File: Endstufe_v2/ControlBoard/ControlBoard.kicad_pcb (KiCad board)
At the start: 4 copper layers, 100 x 85 mm, 231 parts, among them J1 B4B-XH-2_(LF)(SN), J10 DNP, J11 DNP, J12 DNP, J13 DNP, J14 DAC all outputs, J15 B4B-XH-2_(LF)(SN), J16 B6B-XH-2(LF)(SN), J17 Conn_01x02_Pin, J18 Conn_01x02_Pin, J19 Conn_01x06_Pin, J2 B4B-XH-2_(LF)(SN), J3 B4B-XH-2_(LF)(SN), J4 DNP, J5 B6B-XH-2(LF)(SN), J6 Conn_01x02_Pin, J7 DNP, J8 DNP, J9 DNP, SW1 TS-1187A-B-A-B, SW2 TS-1187A-B-A-B, U1 NVTFWS014P04M8LTAG, U10 ADAU1962AWBSTZ, U2 1SMA5927A, U3 TPS62933, U4 TYPE-C 16PFS 2JCB1.2-H6.5 IPX8, U5 W25Q128JVS, U6 RP2040, U7 W25Q128JVS, U8 ADAU1467WBCPZ300, U9 ZPLR135_T8, Y1 12Mhz, Y2 24.576Mhz, Y3 24.576Mhz

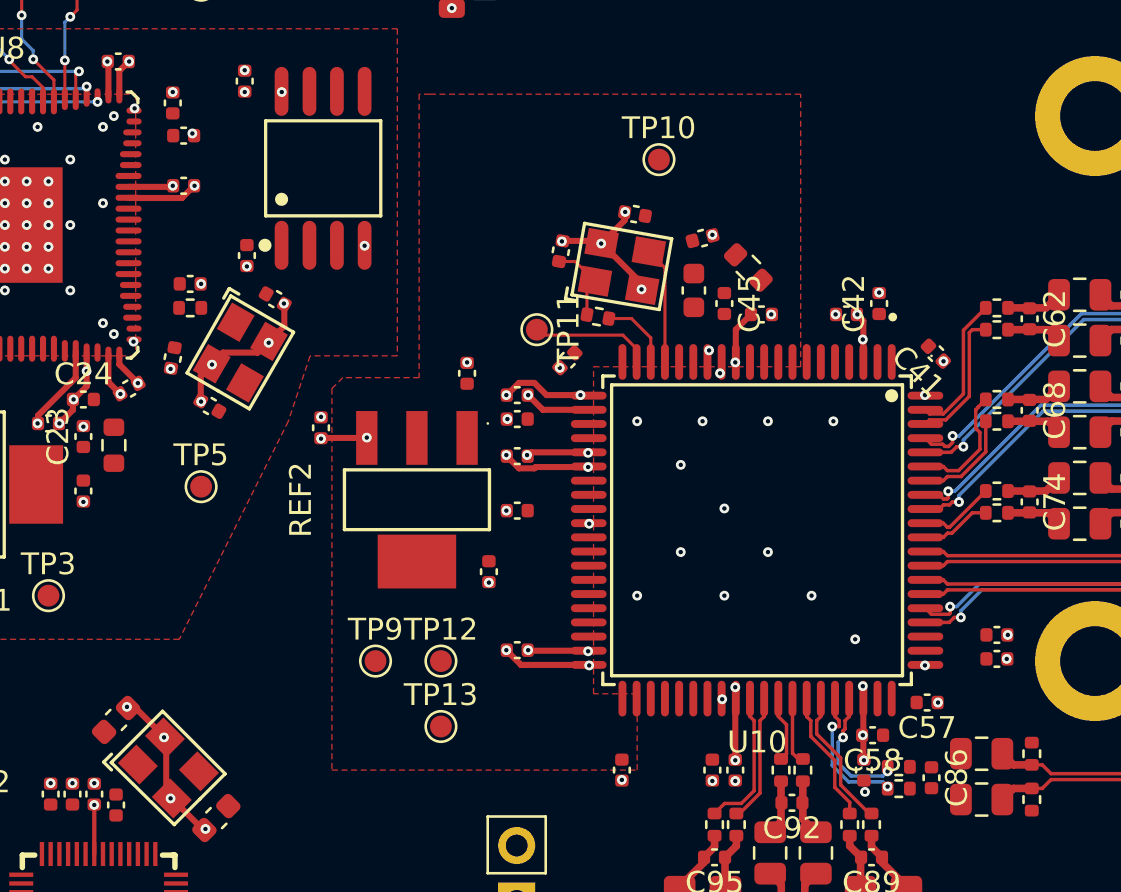
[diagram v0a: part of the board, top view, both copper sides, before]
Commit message: Route control board (continued)
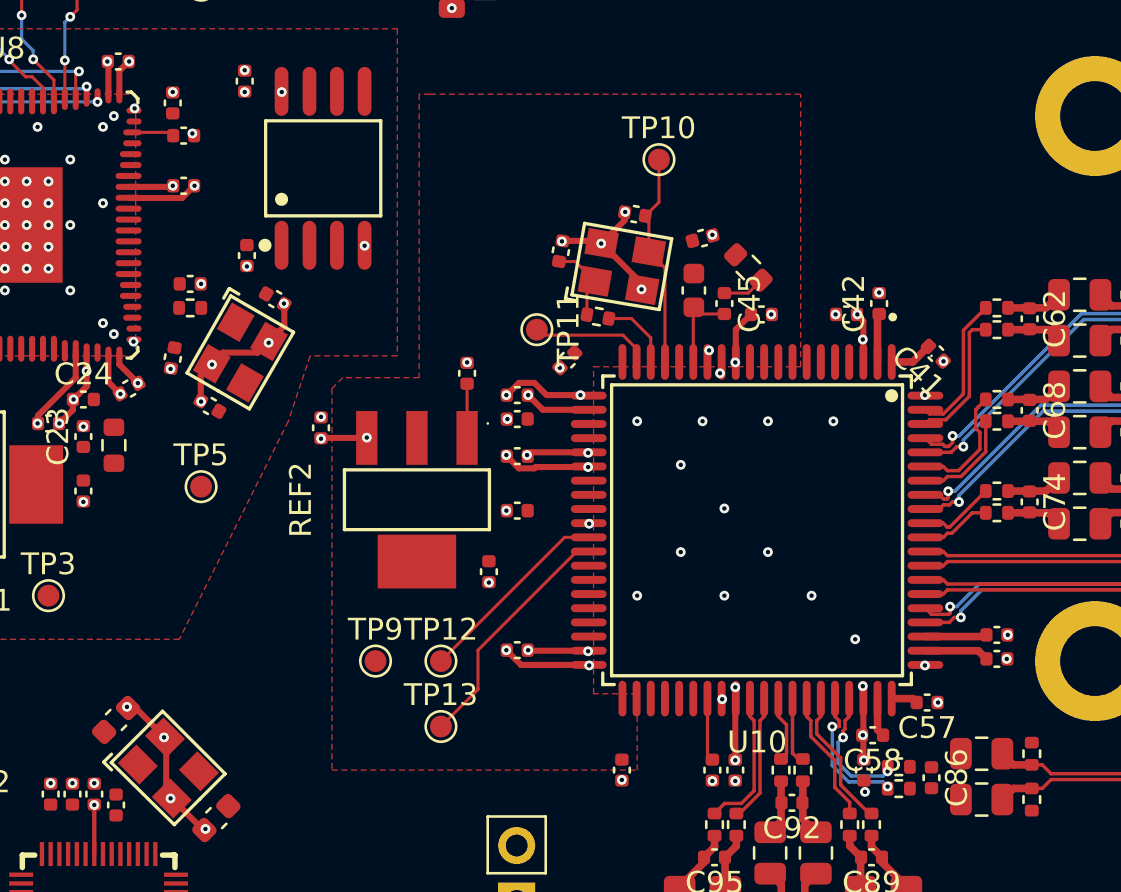
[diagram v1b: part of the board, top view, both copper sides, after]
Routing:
- net Net-(U10-SA2): track 0.00 -> 11.2 mm
- net Net-(U10-SA1): track 0.00 -> 9.13 mm
- net /ADAU1962A/XTALI: track 5.36 -> 9.91 mm
- net /ADAU1962A/LF: track 0.00 -> 4.04 mm
- net /ADAU1962A/CM: track 0.00 -> 2.95 mm
- net /ADAU1962A_RESET: track 0.00 -> 2.89 mm
- net /ADAU1962A/TS_REF: track 0.00 -> 2.83 mm
- net /ADAU1962A/VDRIVE: track 0.00 -> 2.49 mm
- net /ADAU1962A/DAC_BIAS4: track 0.00 -> 2.23 mm
- net /ADAU1962A/DAC_BIAS3: track 0.00 -> 1.98 mm
- net Net-(U8-SELFBOOT): track 0.00 -> 1.93 mm
- net Net-(C45-Pad1): track 0.00 -> 1.93 mm
- net /ADAU1962A/DAC_BIAS1: track 0.00 -> 1.78 mm
- net /ADAU1962A/DAC_BIAS2: track 0.00 -> 1.22 mm

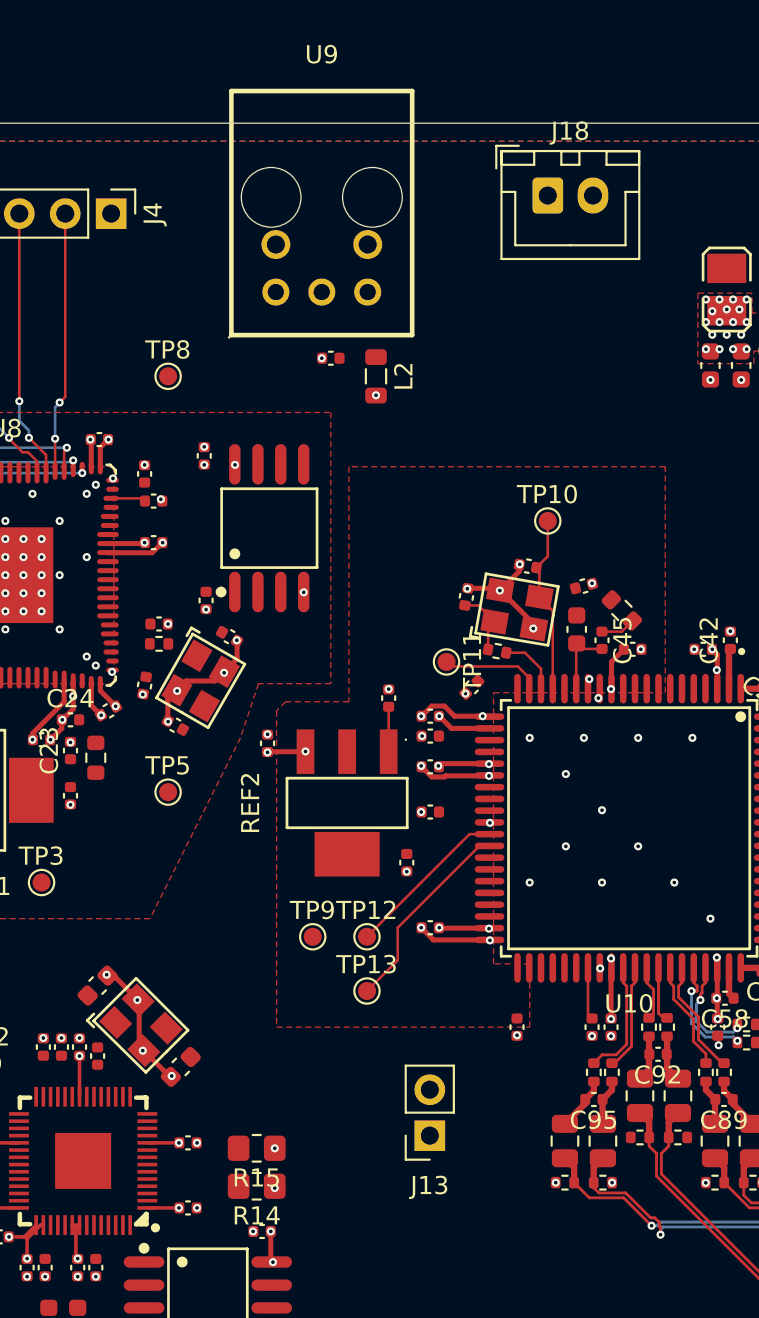
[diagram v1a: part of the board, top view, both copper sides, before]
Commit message: Add missing I2C adress headers and pull down for DAC and DSP
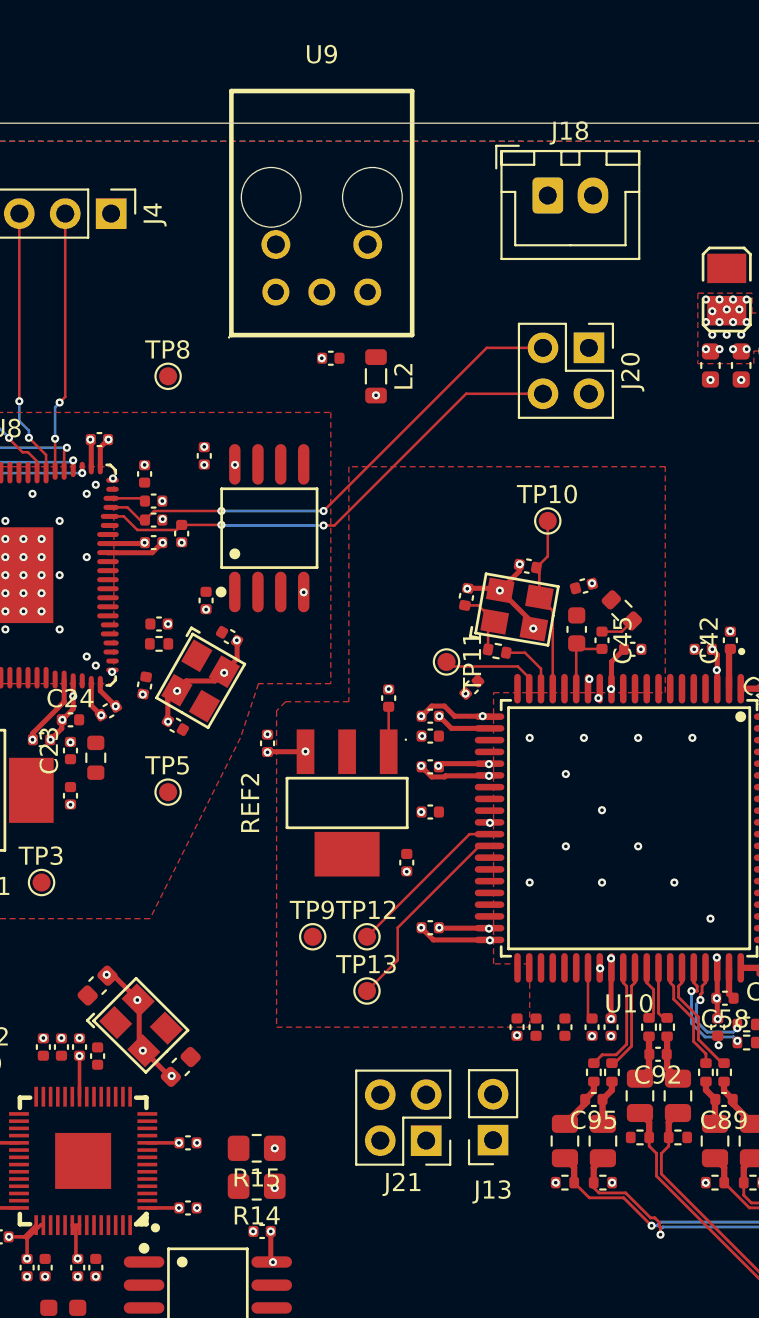
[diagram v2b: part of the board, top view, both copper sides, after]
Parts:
- added J20: DNP, Connector_PinHeader_2.54mm:PinHeader_2x02_P2.54mm_Vertical, F.Cu at (132.3, 82.4)
- added J21: DNP, Connector_PinHeader_2.54mm:PinHeader_2x02_P2.54mm_Vertical, F.Cu at (123.3, 126.3)
- added R74: 10k, Endstufe:C_0402_1005Metric, F.Cu at (109.8, 92.7)
- added R75: 10k, Endstufe:C_0402_1005Metric, F.Cu at (108.2, 92.0)
- added R76: 10k, Endstufe:C_0402_1005Metric, F.Cu at (129.3, 120.0)
- added R77: 10k, Endstufe:C_0402_1005Metric, F.Cu at (130.9, 120.0)
- moved J13 3.51 mm to (127.0, 126.2)
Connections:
- U10 pad 42: /ADAU1962A/ADDR1 -> /ADAU1962A_ADDR1
- U10 pad 45: /ADAU1962A/ADDR0 -> /ADAU1962A_ADDR0
- U8 pad 40: /ADAU1467/ADDR1 -> /ADAU1467_ADDR1
- U8 pad 41: /ADAU1467/ADDR0 -> /ADAU1467_ADDR0
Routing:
- net /ADAU1467_ADDR0: track 0.00 -> 28.2 mm, vias 0 -> 2
- net /ADAU1467_ADDR1: track 0.00 -> 27.5 mm, vias 0 -> 2
- net GND: vias 149 -> 151

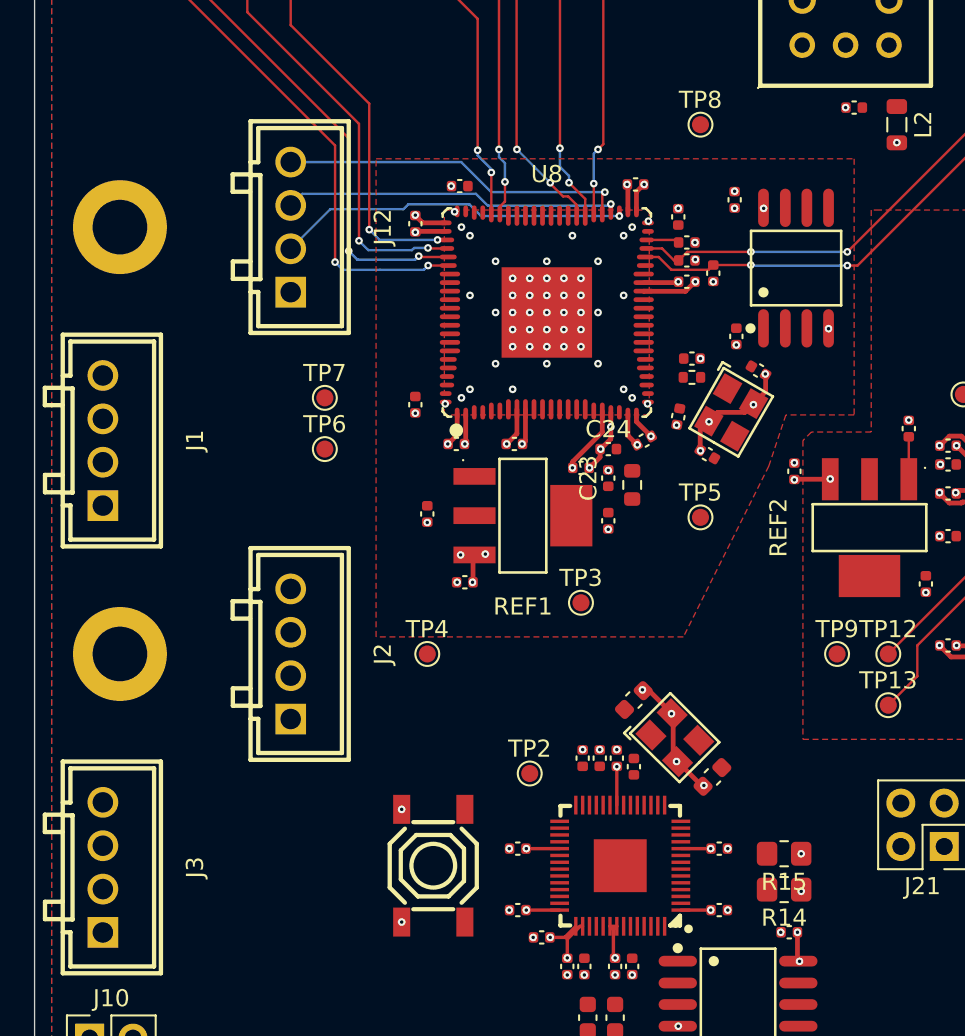
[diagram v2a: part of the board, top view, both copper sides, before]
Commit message: Route control board (continued)
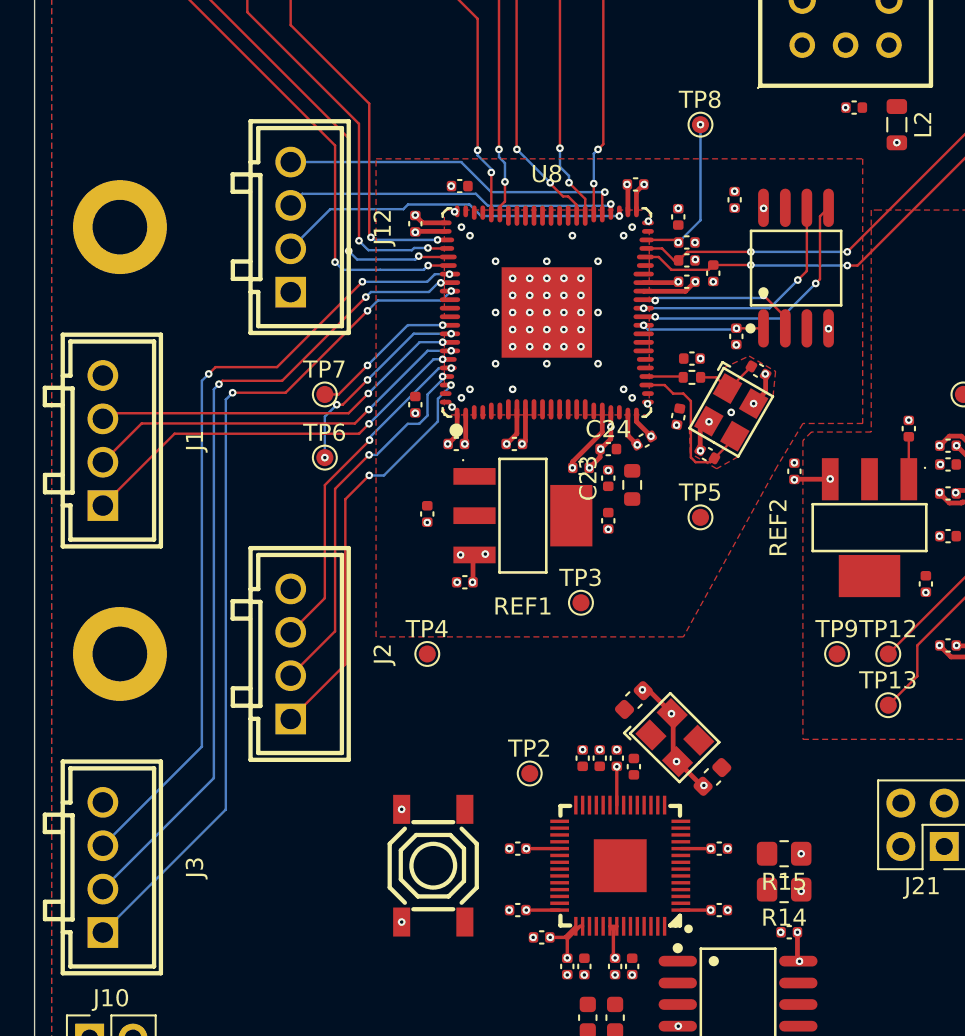
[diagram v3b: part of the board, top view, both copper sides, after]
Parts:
- moved TP6 0.50 mm to (87.0, 103.5)
- moved TP7 0.20 mm to (87.0, 99.8)
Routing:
- net /ADAU1467/ADDITIONAL_SDATA: track 0.00 -> 50.1 mm, vias 0 -> 3
- net /ADAU1467/ADDITIONAL_LRCLK: track 0.00 -> 48.4 mm, vias 0 -> 3
- net /ADAU1467/ADDITIONAL_BLCK: track 0.00 -> 46.7 mm, vias 0 -> 3
- net /ADAU1467/PCM1865_SDATA: track 0.00 -> 24.2 mm, vias 0 -> 2
- net /ADAU1467/PCM9211_SDATA: track 0.00 -> 23.8 mm, vias 0 -> 2
- net /ADAU1467/PCM9211_LRCLK: track 0.00 -> 23.2 mm, vias 0 -> 2
- net /ADAU1467/PCM9211_BLCK: track 0.00 -> 22.2 mm, vias 0 -> 2
- net /ADAU1467/PCM1865_LRCLK: track 0.00 -> 22.1 mm, vias 0 -> 2
- net /ADAU1467/PCM1865_BLCK: track 0.00 -> 20.0 mm, vias 0 -> 2
- net /ADAU1467/SPI_MOSI: track 0.00 -> 15.7 mm, vias 0 -> 2
- net /ADAU1467/SPI_SCLK: track 0.00 -> 14.2 mm, vias 0 -> 2
- net Net-(U8-THD_P): track 0.00 -> 11.9 mm, vias 0 -> 4
- net Net-(U8-XTALIN/MCLK): track 0.00 -> 9.66 mm
- net /ADAU1467/SPI_MISO: track 0.00 -> 9.63 mm, vias 0 -> 2
- net Net-(U8-THD_M): track 0.00 -> 9.01 mm, vias 0 -> 2
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
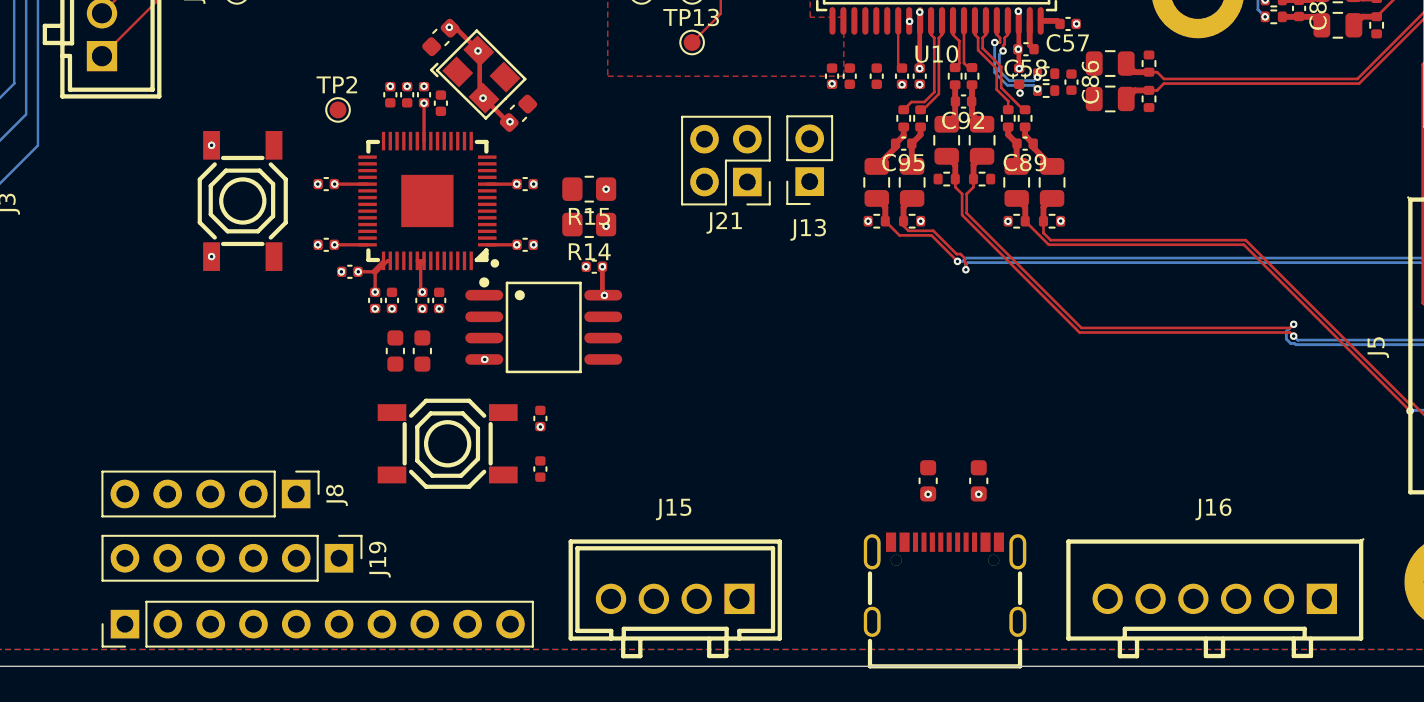
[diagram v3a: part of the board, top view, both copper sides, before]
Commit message: Route control board (continued)
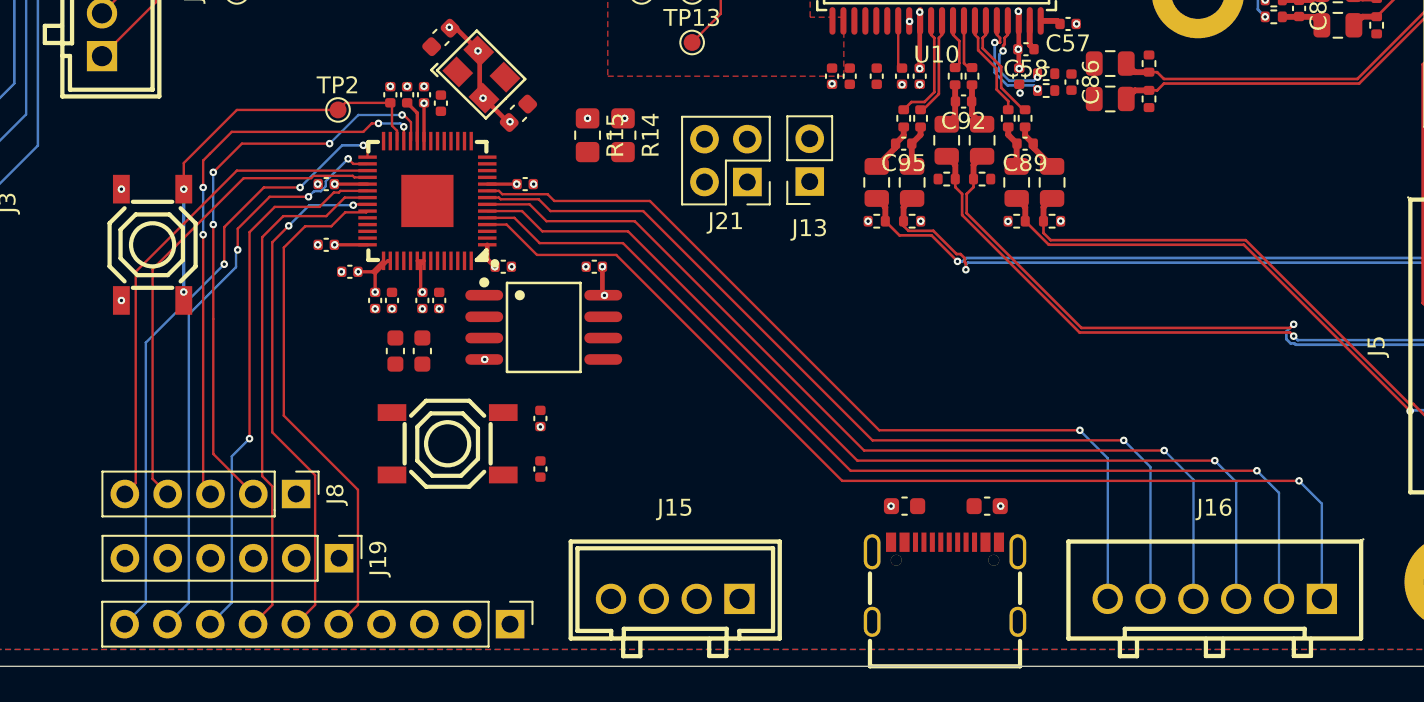
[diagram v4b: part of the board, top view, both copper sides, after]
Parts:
- moved J9 22.8 mm to (109.2, 152.5), turned to -90 degrees
- moved SW2 5.95 mm to (88.0, 130.0)
- moved R14 5.66 mm to (115.9, 123.5), turned to -90 degrees
- moved R15 3.20 mm to (113.8, 123.5), turned to -90 degrees
- moved R8 2.05 mm to (132.6, 145.5), turned to 180 degrees
- moved C12 1.84 mm to (108.8, 131.3)
- moved R7 1.58 mm to (137.5, 145.5), turned to 0 degrees
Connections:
- J8 pad 4: /RP2040/GPIO20_UART_TX -> /RP2040/GPIO21_UART_RX
- J8 pad 5: /RP2040/GPIO21_UART_RX -> /RP2040/GPIO20_UART_TX
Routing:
- net /SDZA: track 0.00 -> 62.0 mm, vias 0 -> 1
- net /SDZB: track 0.00 -> 60.0 mm, vias 0 -> 1
- net /FAULTZA: track 0.00 -> 58.0 mm, vias 0 -> 1
- net /FAULTZB: track 0.00 -> 55.7 mm, vias 0 -> 1
- net /MUTEA: track 0.00 -> 53.8 mm, vias 0 -> 1
- net /MUTEB: track 0.00 -> 51.7 mm, vias 0 -> 1
- net Net-(J9-Pin_10): track 0.00 -> 37.1 mm, vias 0 -> 3
- net Net-(J9-Pin_9): track 0.00 -> 34.9 mm, vias 0 -> 3
- net Net-(J8-Pin_2): track 0.00 -> 34.5 mm, vias 0 -> 4
- net Net-(J8-Pin_3): track 0.00 -> 33.7 mm, vias 0 -> 4
- net Net-(J9-Pin_8): track 0.00 -> 32.2 mm, vias 0 -> 1
- net Net-(J9-Pin_7): track 0.00 -> 31.0 mm
- net Net-(J9-Pin_6): track 0.00 -> 30.8 mm, vias 0 -> 2
- net Net-(J9-Pin_5): track 0.00 -> 30.5 mm
- net /RP2040/GPIO20_UART_TX: track 0.00 -> 29.7 mm
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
